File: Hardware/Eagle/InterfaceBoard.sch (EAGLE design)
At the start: 20 parts

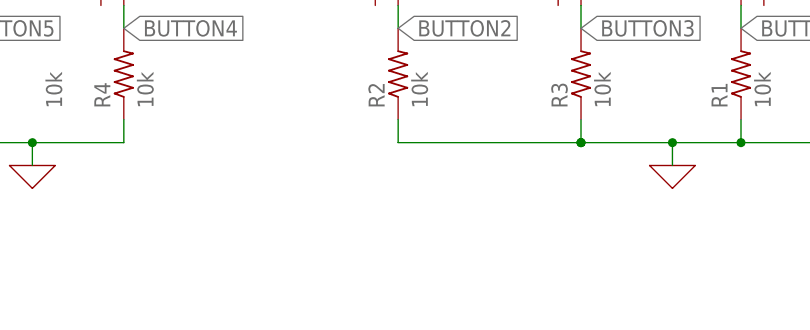
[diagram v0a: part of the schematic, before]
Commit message: added 'designed by' in schematic
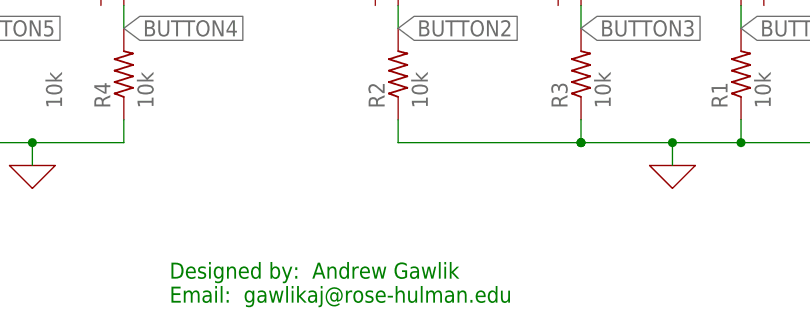
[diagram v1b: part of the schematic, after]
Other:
- note added: "Designed by: Andrew Gawlik Email: gawlikaj@rose-hulman.edu"
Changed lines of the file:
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@@
 <sheet>
 <plain>
+<text x="86.36" y="15.24" size="1.778" layer="91">Designed by:  Andrew Gawlik
+Email:  gawlikaj@rose-hulman.edu</text>
 </plain>
 <instances>
@@
 </drawing>
 <compatibility>
+<note version="6.3" minversion="6.2.2" severity="warning">
+Since Version 6.2.2 text objects can contain more than one line,
+which will not be processed correctly with this version.
+</note>
 <note version="8.2" severity="warning">
 Since Version 8.2, EAGLE supports online libraries. The ids

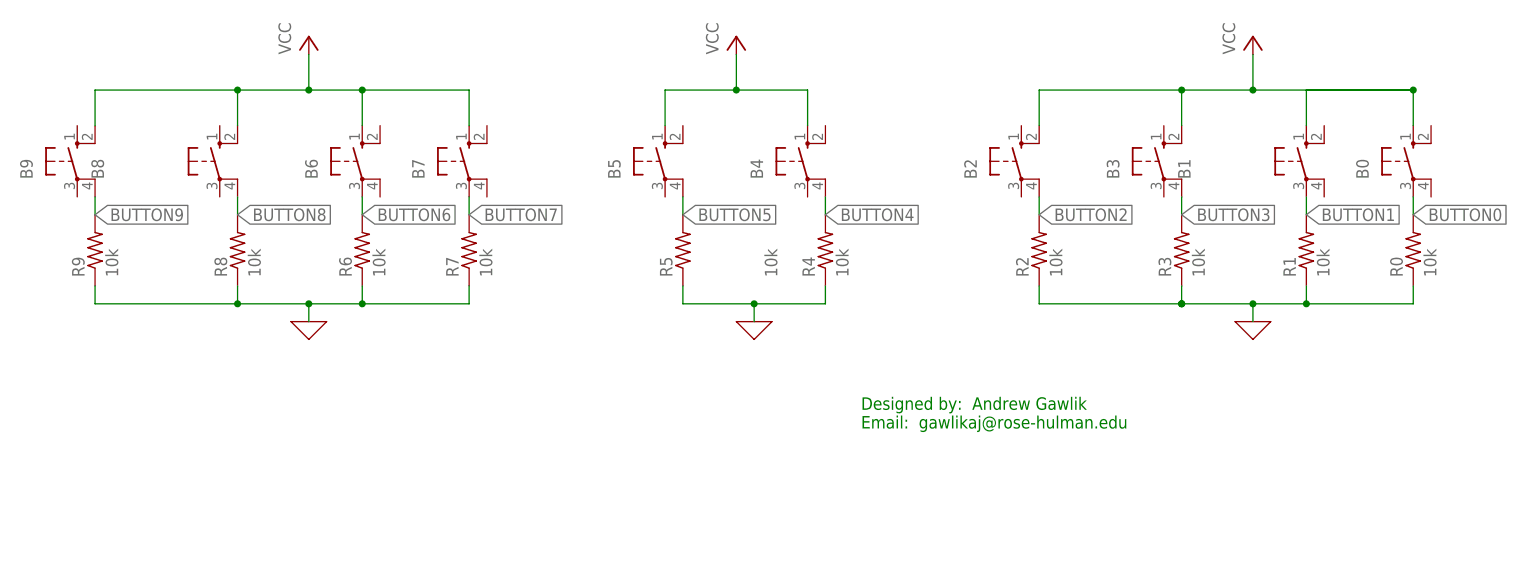
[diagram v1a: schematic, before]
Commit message: Specified button colors and added Designed by in the PCB layout
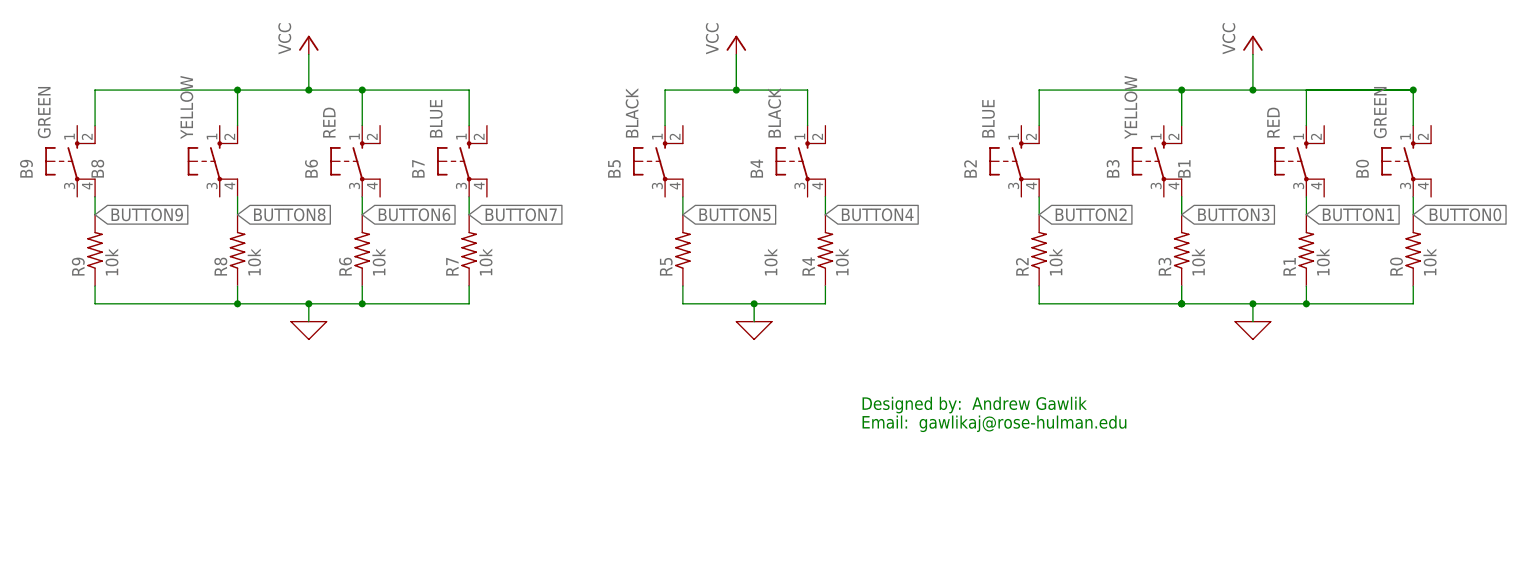
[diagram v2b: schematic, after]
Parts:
- B0, B9: value (none) -> GREEN
- B1, B6: value (none) -> RED
- B2, B7: value (none) -> BLUE
- B3, B8: value (none) -> YELLOW
- B4, B5: value (none) -> BLACK
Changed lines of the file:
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@@
 </groups>
 <parts>
-<part name="B9" library="switch-omron" library_urn="urn:adsk.eagle:library:377" deviceset="10-XX" device="" package3d_urn="urn:adsk.eagle:package:27496/1"/>
-<part name="B6" library="switch-omron" library_urn="urn:adsk.eagle:library:377" deviceset="10-XX" device="" package3d_urn="urn:adsk.eagle:package:27496/1"/>
-<part name="B7" library="switch-omron" library_urn="urn:adsk.eagle:library:377" deviceset="10-XX" device="" package3d_urn="urn:adsk.eagle:package:27496/1"/>
-<part name="B8" library="switch-omron" library_urn="urn:adsk.eagle:library:377" deviceset="10-XX" device="" package3d_urn="urn:adsk.eagle:package:27496/1"/>
+<part name="B9" library="switch-omron" library_urn="urn:adsk.eagle:library:377" deviceset="10-XX" device="" package3d_urn="urn:adsk.eagle:package:27496/1" value="GREEN"/>
+<part name="B6" library="switch-omron" library_urn="urn:adsk.eagle:library:377" deviceset="10-XX" device="" package3d_urn="urn:adsk.eagle:package:27496/1" value="RED"/>
+<part name="B7" library="switch-omron" library_urn="urn:adsk.eagle:library:377" deviceset="10-XX" device="" package3d_urn="urn:adsk.eagle:package:27496/1" value="BLUE"/>
+<part name="B8" library="switch-omron" library_urn="urn:adsk.eagle:library:377" deviceset="10-XX" device="" package3d_urn="urn:adsk.eagle:package:27496/1" value="YELLOW"/>
 <part name="R8" library="rcl" library_urn="urn:adsk.eagle:library:334" deviceset="R-US_" device="0204/5" package3d_urn="urn:adsk.eagle:package:23488/1" value="10k"/>
 <part name="R7" library="rcl" library_urn="urn:adsk.eagle:library:334" deviceset="R-US_" device="0204/5" package3d_urn="urn:adsk.eagle:package:23488/1" value="10k"/>
@@
 <part name="X_1" library="ngspice-simulation" library_urn="urn:adsk.eagle:library:527439" deviceset="GND" device=""/>
 <part name="P+1" library="supply1" library_urn="urn:adsk.eagle:library:371" deviceset="VCC" device=""/>
-<part name="B2" library="switch-omron" library_urn="urn:adsk.eagle:library:377" deviceset="10-XX" device="" package3d_urn="urn:adsk.eagle:package:27496/1"/>
-<part name="B3" library="switch-omron" library_urn="urn:adsk.eagle:library:377" deviceset="10-XX" device="" package3d_urn="urn:adsk.eagle:package:27496/1"/>
-<part name="B0" library="switch-omron" library_urn="urn:adsk.eagle:library:377" deviceset="10-XX" device="" package3d_urn="urn:adsk.eagle:package:27496/1"/>
-<part name="B1" library="switch-omron" library_urn="urn:adsk.eagle:library:377" deviceset="10-XX" device="" package3d_urn="urn:adsk.eagle:package:27496/1"/>
+<part name="B2" library="switch-omron" library_urn="urn:adsk.eagle:library:377" deviceset="10-XX" device="" package3d_urn="urn:adsk.eagle:package:27496/1" value="BLUE"/>
+<part name="B3" library="switch-omron" library_urn="urn:adsk.eagle:library:377" deviceset="10-XX" device="" package3d_urn="urn:adsk.eagle:package:27496/1" value="YELLOW"/>
+<part name="B0" library="switch-omron" library_urn="urn:adsk.eagle:library:377" deviceset="10-XX" device="" package3d_urn="urn:adsk.eagle:package:27496/1" value="GREEN"/>
+<part name="B1" library="switch-omron" library_urn="urn:adsk.eagle:library:377" deviceset="10-XX" device="" package3d_urn="urn:adsk.eagle:package:27496/1" value="RED"/>
 <part name="R1" library="rcl" library_urn="urn:adsk.eagle:library:334" deviceset="R-US_" device="0204/5" package3d_urn="urn:adsk.eagle:package:23488/1" value="10k"/>
 <part name="R0" library="rcl" library_urn="urn:adsk.eagle:library:334" deviceset="R-US_" device="0204/5" package3d_urn="urn:adsk.eagle:package:23488/1" value="10k"/>
@@
 <part name="X_3" library="ngspice-simulation" library_urn="urn:adsk.eagle:library:527439" deviceset="GND" device=""/>
 <part name="P+3" library="supply1" library_urn="urn:adsk.eagle:library:371" deviceset="VCC" device=""/>
-<part name="B5" library="switch-omron" library_urn="urn:adsk.eagle:library:377" deviceset="10-XX" device="" package3d_urn="urn:adsk.eagle:package:27496/1"/>
-<part name="B4" library="switch-omron" library_urn="urn:adsk.eagle:library:377" deviceset="10-XX" device="" package3d_urn="urn:adsk.eagle:package:27496/1"/>
+<part name="B5" library="switch-omron" library_urn="urn:adsk.eagle:library:377" deviceset="10-XX" device="" package3d_urn="urn:adsk.eagle:package:27496/1" value="BLACK"/>
+<part name="B4" library="switch-omron" library_urn="urn:adsk.eagle:library:377" deviceset="10-XX" device="" package3d_urn="urn:adsk.eagle:package:27496/1" value="BLACK"/>
 <part name="R4" library="rcl" library_urn="urn:adsk.eagle:library:334" deviceset="R-US_" device="0204/5" package3d_urn="urn:adsk.eagle:package:23488/1" value="10k"/>
 <part name="R5" library="rcl" library_urn="urn:adsk.eagle:library:334" deviceset="R-US_" device="0204/5" package3d_urn="urn:adsk.eagle:package:23488/1" value="10k"/>

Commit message: Added speakers to PCB layout
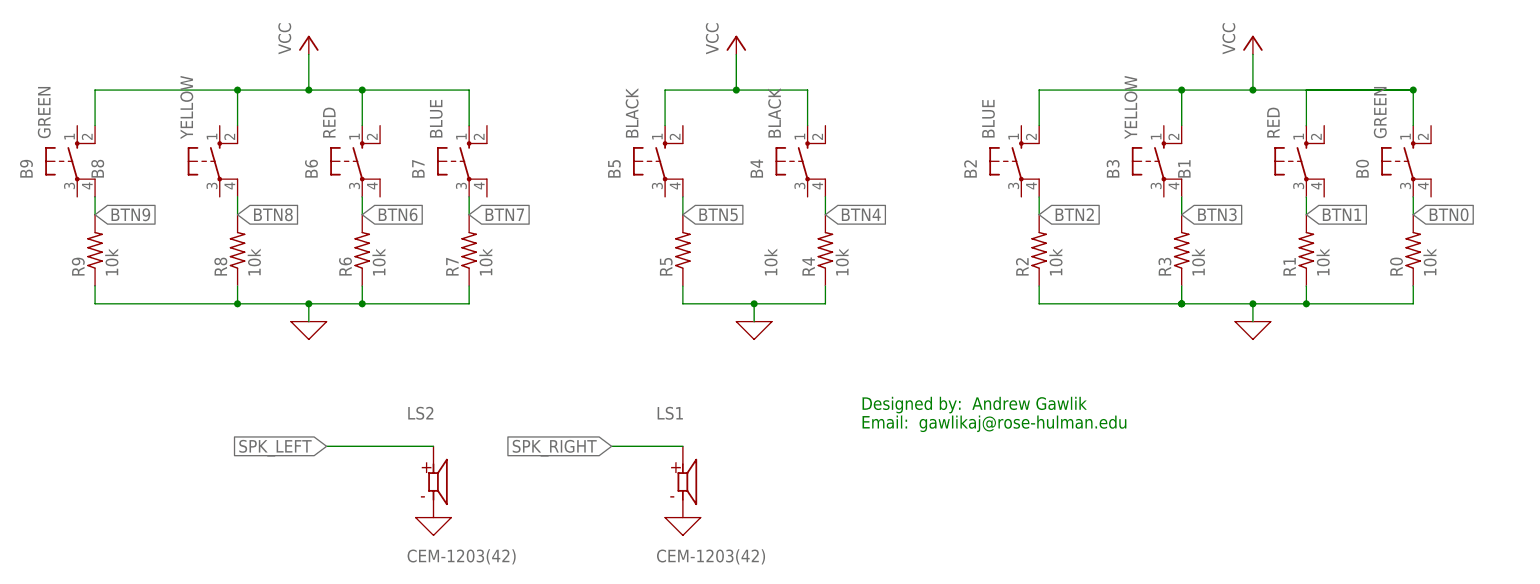
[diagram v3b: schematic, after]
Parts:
- added LS1, LS2: CEM-1203(42), CEM-1203_42_:CEM-1203(42)
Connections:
- net BUTTON0 renamed BTN0
- net BUTTON1 renamed BTN1
- net BUTTON2 renamed BTN2
- net BUTTON3 renamed BTN3
- net BUTTON4 renamed BTN4
- net BUTTON5 renamed BTN5
- net BUTTON6 renamed BTN6
- net BUTTON7 renamed BTN7
- net BUTTON8 renamed BTN8
- net BUTTON9 renamed BTN9
- new net SPK_LEFT: LS2.P
- new net SPK_RIGHT: LS1.P
- net 0: now also LS1.N, LS2.N
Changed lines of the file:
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@@
 <part name="X_2" library="ngspice-simulation" library_urn="urn:adsk.eagle:library:527439" deviceset="GND" device=""/>
 <part name="P+2" library="supply1" library_urn="urn:adsk.eagle:library:371" deviceset="VCC" device=""/>
-<part name="FRAME1" library="frames" library_urn="urn:adsk.eagle:library:229" deviceset="LETTER_L" device=""/>
+<part name="FRAME1" library="frames" library_urn="urn:adsk.eagle:library:229" deviceset="LETTER_L" device="" value="Page1 "/>
+<part name="LS1" library="CEM-1203_42_" deviceset="CEM-1203(42)" device=""/>
+<part name="LS2" library="CEM-1203_42_" deviceset="CEM-1203(42)" device=""/>
+<part name="X_4" library="ngspice-simulation" library_urn="urn:adsk.eagle:library:527439" deviceset="GND" device=""/>
+<part name="X_5" library="ngspice-simulation" library_urn="urn:adsk.eagle:library:527439" deviceset="GND" device=""/>
 </parts>
 <sheets>
@@
 <attribute name="DRAWING_NAME" x="101.6" y="6.35" size="2.54" layer="94"/>
 </instance>
+<instance part="LS1" gate="G$1" x="60.96" y="7.62" smashed="yes">
+<attribute name="NAME" x="57.144509375" y="16.52281875" size="1.78056875" layer="95"/>
+<attribute name="VALUE" x="57.1442" y="-3.8275" size="1.780709375" layer="96"/>
+</instance>
+<instance part="LS2" gate="G$1" x="25.4" y="7.62" smashed="yes">
+<attribute name="NAME" x="21.584509375" y="16.52281875" size="1.78056875" layer="95"/>
+<attribute name="VALUE" x="21.5842" y="-3.8275" size="1.780709375" layer="96"/>
+</instance>
+<instance part="X_4" gate="G$1" x="25.4" y="2.54" smashed="yes"/>
+<instance part="X_5" gate="G$1" x="60.96" y="2.54" smashed="yes"/>
 </instances>
 <busses>
@@
 <junction x="7.62" y="33.02" grouprefs="LEFTBUTTONS"/>
 </segment>
-</net>
-<net name="BUTTON9" class="0">
+<segment>
+<pinref part="X_4" gate="G$1" pin="0"/>
+<pinref part="LS2" gate="G$1" pin="N"/>
+</segment>
+<segment>
+<pinref part="X_5" gate="G$1" pin="0"/>
+<pinref part="LS1" gate="G$1" pin="N"/>
+</segment>
+</net>
+<net name="BTN9" class="0">
 <segment>
 <pinref part="R9" gate="G$1" pin="2"/>
@@
 </segment>
 </net>
-<net name="BUTTON7" class="0">
+<net name="BTN7" class="0">
 <segment>
 <pinref part="R7" gate="G$1" pin="2"/>
@@
 </segment>
 </net>
-<net name="BUTTON2" class="0">
+<net name="BTN2" class="0">
 <segment>
 <pinref part="R2" gate="G$1" pin="2"/>
@@
 </segment>
 </net>
-<net name="BUTTON3" class="0">
+<net name="BTN3" class="0">
 <segment>
 <pinref part="R3" gate="G$1" pin="2"/>
@@
 </segment>
 </net>
-<net name="BUTTON0" class="0">
+<net name="BTN0" class="0">
 <segment>
 <pinref part="R0" gate="G$1" pin="2"/>
@@
 </segment>
 </net>
-<net name="BUTTON1" class="0">
+<net name="BTN1" class="0">
 <segment>
 <pinref part="R1" gate="G$1" pin="2"/>
@@
 </segment>
 </net>
-<net name="BUTTON5" class="0">
+<net name="BTN5" class="0">
 <segment>
 <pinref part="R5" gate="G$1" pin="2"/>
@@
 </segment>
 </net>
-<net name="BUTTON4" class="0">
+<net name="BTN4" class="0">
 <segment>
 <pinref part="R4" gate="G$1" pin="2"/>
@@
 </segment>
 </net>
-<net name="BUTTON8" class="0">
+<net name="BTN8" class="0">
 <segment>
 <pinref part="R8" gate="G$1" pin="2"/>
@@
 </segment>
 </net>
-<net name="BUTTON6" class="0">
+<net name="BTN6" class="0">
 <segment>
 <pinref part="B6" gate="1" pin="P"/>
@@
 </segment>
 </net>
+<net name="SPK_LEFT" class="0">
+<segment>
+<pinref part="LS2" gate="G$1" pin="P"/>
+<wire x1="25.4" y1="12.7" x2="10.16" y2="12.7" width="0.1524" layer="91"/>
+<label x="10.16" y="12.7" size="1.778" layer="95" rot="R180" xref="yes"/>
+</segment>
+</net>
+<net name="SPK_RIGHT" class="0">
+<segment>
+<pinref part="LS1" gate="G$1" pin="P"/>
+<wire x1="60.96" y1="12.7" x2="50.8" y2="12.7" width="0.1524" layer="91"/>
+<label x="50.8" y="12.7" size="1.778" layer="95" rot="R180" xref="yes"/>
+</segment>
+</net>
